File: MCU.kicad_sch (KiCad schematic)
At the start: 26 parts, among them U5 ESP32-D0WD, U6 W25Q128JVP, U7 APS6404L-3SQR-ZR, Y2 40.000 MHz

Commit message: updated Mouser part number for PSRAM
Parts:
- U7: MOUSER# 878-APS6404L-3SQR-ZR -> 878-APS6404L-3SQR-SN
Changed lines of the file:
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@@
 			)
 		)
-		(property "Datasheet" "~"
+		(property "Datasheet" "Data Sheets\\abm8-1384678.pdf"
 			(at 128.27 163.83 0)
 			(effects
@@
 			)
 		)
-		(property "Datasheet" "https://www.mouser.com/datasheet/2/1127/APM_PSRAM_QSPI_APS6404L_3SQR_v2_3_PKG-1954826.pdf"
+		(property "Datasheet" "Data Sheets\\APM_PSRAM_E3_QSPI__APS6404L_3SQR_KGD_PKG__v2.7.pdf"
 			(at 50.8 129.54 0)
 			(effects
@@
 			)
 		)
-		(property "MOUSER#" "878-APS6404L-3SQR-ZR"
+		(property "MOUSER#" "878-APS6404L-3SQR-SN"
 			(at 50.8 111.76 0)
 			(effects

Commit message: all parts geo-renamed
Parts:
- renumbered C49 to 1C10, C39 to 1C11, C38 to 1C12, R28 to 1R2, R45 to 1R3, R39 to 1R6, R41 to 1R8, U6 to 1U2, U5 to 1U4, C50 to 2C15, C22 to 2C16, C47 to 2C23, C20 to 2C26, C44 to 2C28, C48 to 2C29, C42 to 2C30, C19 to 2C31, C46 to 2C32, C41 to 2C33, C21 to 2C35, C45 to 2C36, C43 to 2C37, R42 to 2R20, R40 to 2R36, U7 to 2U3, Y2 to 2Y2
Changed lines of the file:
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@@
 		(on_board yes)
 		(dnp no)
-		(property "Reference" "C39"
+		(property "Reference" "1C11"
 			(at 116.84 44.4499 0)
 			(effects
@@
 			(project "ESP32PoE"
 				(path "/4c939de5-59ef-438d-9f29-5de1016e5f2f/9bdf3d9b-885e-428e-95ba-d4f7bd684dc5"
-					(reference "C39")
+					(reference "1C11")
 					(unit 1)
 				)
@@
 		(dnp no)
 		(fields_autoplaced yes)
-		(property "Reference" "C20"
+		(property "Reference" "2C26"
 			(at 139.7 171.4499 0)
 			(effects
@@
 			(project "ESP32PoE"
 				(path "/4c939de5-59ef-438d-9f29-5de1016e5f2f/9bdf3d9b-885e-428e-95ba-d4f7bd684dc5"
-					(reference "C20")
+					(reference "2C26")
 					(unit 1)
 				)
@@
 		(dnp no)
 		(fields_autoplaced yes)
-		(property "Reference" "R42"
+		(property "Reference" "2R20"
 			(at 39.37 96.5199 0)
 			(effects
@@
 			(project "ESP32PoE"
 				(path "/4c939de5-59ef-438d-9f29-5de1016e5f2f/9bdf3d9b-885e-428e-95ba-d4f7bd684dc5"
-					(reference "R42")
+					(reference "2R20")
 					(unit 1)
 				)
@@
 		(dnp no)
 		(fields_autoplaced yes)
-		(property "Reference" "Y2"
+		(property "Reference" "2Y2"
 			(at 139.7 157.4098 0)
 			(effects
@@
 			(project ""
 				(path "/4c939de5-59ef-438d-9f29-5de1016e5f2f/9bdf3d9b-885e-428e-95ba-d4f7bd684dc5"
-					(reference "Y2")
+					(reference "2Y2")
 					(unit 1)
 				)
@@
 		(dnp no)
 		(fields_autoplaced yes)
-		(property "Reference" "U5"
+		(property "Reference" "1U4"
 			(at 218.44 29.21 0)
 			(effects
@@
 			(project ""
 				(path "/4c939de5-59ef-438d-9f29-5de1016e5f2f/9bdf3d9b-885e-428e-95ba-d4f7bd684dc5"
-					(reference "U5")
+					(reference "1U4")
 					(unit 1)
 				)
@@
 		(dnp no)
 		(fields_autoplaced yes)
-		(property "Reference" "C38"
+		(property "Reference" "1C12"
 			(at 191.77 41.9099 0)
 			(effects
@@
 			(project "ESP32PoE"
 				(path "/4c939de5-59ef-438d-9f29-5de1016e5f2f/9bdf3d9b-885e-428e-95ba-d4f7bd684dc5"
-					(reference "C38")
+					(reference "1C12")
 					(unit 1)
 				)
@@
 		(dnp no)
 		(fields_autoplaced yes)
-		(property "Reference" "R28"
+		(property "Reference" "1R2"
 			(at 264.16 91.44 90)
 			(effects
@@
 			(project "ESP32PoE"
 				(path "/4c939de5-59ef-438d-9f29-5de1016e5f2f/9bdf3d9b-885e-428e-95ba-d4f7bd684dc5"
-					(reference "R28")
+					(reference "1R2")
 					(unit 1)
 				)
@@
 		(on_board yes)
 		(dnp no)
-		(property "Reference" "C21"
+		(property "Reference" "2C35"
 			(at 121.92 113.0299 0)
 			(effects
@@
 			(project "ESP32PoE"
 				(path "/4c939de5-59ef-438d-9f29-5de1016e5f2f/9bdf3d9b-885e-428e-95ba-d4f7bd684dc5"
-					(reference "C21")
+					(reference "2C35")
 					(unit 1)
 				)
@@
 		(dnp no)
 		(fields_autoplaced yes)
-		(property "Reference" "C49"
+		(property "Reference" "1C10"
 			(at 127 44.4499 0)
 			(effects
@@
 			(project "ESP32PoE"
 				(path "/4c939de5-59ef-438d-9f29-5de1016e5f2f/9bdf3d9b-885e-428e-95ba-d4f7bd684dc5"
-					(reference "C49")
+					(reference "1C10")
 					(unit 1)
 				)
@@
 		(on_board yes)
 		(dnp no)
-		(property "Reference" "C45"
+		(property "Reference" "2C36"
 			(at 33.02 59.6899 0)
 			(effects
@@
 			(project "ESP32PoE"
 				(path "/4c939de5-59ef-438d-9f29-5de1016e5f2f/9bdf3d9b-885e-428e-95ba-d4f7bd684dc5"
-					(reference "C45")
+					(reference "2C36")
 					(unit 1)
 				)
@@
 		(on_board yes)
 		(dnp no)
-		(property "Reference" "C19"
+		(property "Reference" "2C31"
 			(at 112.014 171.45 0)
 			(effects
@@
 			(project ""
 				(path "/4c939de5-59ef-438d-9f29-5de1016e5f2f/9bdf3d9b-885e-428e-95ba-d4f7bd684dc5"
-					(reference "C19")
+					(reference "2C31")
 					(unit 1)
 				)
@@
 		(dnp no)
 		(fields_autoplaced yes)
-		(property "Reference" "R39"
+		(property "Reference" "1R6"
 			(at 114.3 157.48 90)
 			(effects
@@
 			(project ""
 				(path "/4c939de5-59ef-438d-9f29-5de1016e5f2f/9bdf3d9b-885e-428e-95ba-d4f7bd684dc5"
-					(reference "R39")
+					(reference "1R6")
 					(unit 1)
 				)
@@
 		(on_board yes)
 		(dnp no)
-		(property "Reference" "C22"
+		(property "Reference" "2C16"
 			(at 139.7 44.4499 0)
 			(effects
@@
 			(project "ESP32PoE"
 				(path "/4c939de5-59ef-438d-9f29-5de1016e5f2f/9bdf3d9b-885e-428e-95ba-d4f7bd684dc5"
-					(reference "C22")
+					(reference "2C16")
 					(unit 1)
 				)
@@
 		(dnp no)
 		(fields_autoplaced yes)
-		(property "Reference" "U7"
+		(property "Reference" "2U3"
 			(at 59.69 110.4899 0)
 			(effects
@@
 			(project ""
 				(path "/4c939de5-59ef-438d-9f29-5de1016e5f2f/9bdf3d9b-885e-428e-95ba-d4f7bd684dc5"
-					(reference "U7")
+					(reference "2U3")
 					(unit 1)
 				)
@@
 		(dnp no)
 		(fields_autoplaced yes)
-		(property "Reference" "R40"
+		(property "Reference" "2R36"
 			(at 120.65 102.8699 0)
 			(effects
@@
 			(project "ESP32PoE"
 				(path "/4c939de5-59ef-438d-9f29-5de1016e5f2f/9bdf3d9b-885e-428e-95ba-d4f7bd684dc5"
-					(reference "R40")
+					(reference "2R36")
 					(unit 1)
 				)
@@
 		(dnp no)
 		(fields_autoplaced yes)
-		(property "Reference" "C42"
+		(property "Reference" "2C30"
 			(at 45.72 36.8299 0)
 			(effects
@@
 			(project "ESP32PoE"
 				(path "/4c939de5-59ef-438d-9f29-5de1016e5f2f/9bdf3d9b-885e-428e-95ba-d4f7bd684dc5"
-					(reference "C42")
+					(reference "2C30")
 					(unit 1)
 				)
@@
 		(on_board yes)
 		(dnp no)
-		(property "Reference" "C43"
+		(property "Reference" "2C37"
 			(at 71.12 36.8299 0)
 			(effects
@@
 			(project "ESP32PoE"
 				(path "/4c939de5-59ef-438d-9f29-5de1016e5f2f/9bdf3d9b-885e-428e-95ba-d4f7bd684dc5"
-					(reference "C43")
+					(reference "2C37")
 					(unit 1)
 				)
@@
 		(dnp no)
 		(fields_autoplaced yes)
-		(property "Reference" "C50"
+		(property "Reference" "2C15"
 			(at 149.86 44.4499 0)
 			(effects
@@
 			(project "ESP32PoE"
 				(path "/4c939de5-59ef-438d-9f29-5de1016e5f2f/9bdf3d9b-885e-428e-95ba-d4f7bd684dc5"
-					(reference "C50")
+					(reference "2C15")
 					(unit 1)
 				)
@@
 		(dnp no)
 		(fields_autoplaced yes)
-		(property "Reference" "C41"
+		(property "Reference" "2C33"
 			(at 33.02 36.8299 0)
 			(effects
@@
 			(project "ESP32PoE"
 				(path "/4c939de5-59ef-438d-9f29-5de1016e5f2f/9bdf3d9b-885e-428e-95ba-d4f7bd684dc5"
-					(reference "C41")
+					(reference "2C33")
 					(unit 1)
 				)
@@
 		(dnp no)
 		(fields_autoplaced yes)
-		(property "Reference" "R45"
+		(property "Reference" "1R3"
 			(at 177.8 118.1099 0)
 			(effects
@@
 			(project "ESP32PoE"
 				(path "/4c939de5-59ef-438d-9f29-5de1016e5f2f/9bdf3d9b-885e-428e-95ba-d4f7bd684dc5"
-					(reference "R45")
+					(reference "1R3")
 					(unit 1)
 				)
@@
 		(dnp no)
 		(fields_autoplaced yes)
-		(property "Reference" "C47"
+		(property "Reference" "2C23"
 			(at 74.93 58.4199 0)
 			(effects
@@
 			(project "ESP32PoE"
 				(path "/4c939de5-59ef-438d-9f29-5de1016e5f2f/9bdf3d9b-885e-428e-95ba-d4f7bd684dc5"
-					(reference "C47")
+					(reference "2C23")
 					(unit 1)
 				)
@@
 		(dnp no)
 		(fields_autoplaced yes)
-		(property "Reference" "C44"
+		(property "Reference" "2C28"
 			(at 58.42 36.8299 0)
 			(effects
@@
 			(project "ESP32PoE"
 				(path "/4c939de5-59ef-438d-9f29-5de1016e5f2f/9bdf3d9b-885e-428e-95ba-d4f7bd684dc5"
-					(reference "C44")
+					(reference "2C28")
 					(unit 1)
 				)
@@
 		(dnp no)
 		(fields_autoplaced yes)
-		(property "Reference" "R41"
+		(property "Reference" "1R8"
 			(at 190.5 128.2699 0)
 			(effects
@@
 			(project "ESP32PoE"
 				(path "/4c939de5-59ef-438d-9f29-5de1016e5f2f/9bdf3d9b-885e-428e-95ba-d4f7bd684dc5"
-					(reference "R41")
+					(reference "1R8")
 					(unit 1)
 				)
@@
 		(dnp no)
 		(fields_autoplaced yes)
-		(property "Reference" "C46"
+		(property "Reference" "2C32"
 			(at 44.45 59.6899 0)
 			(effects
@@
 			(project "ESP32PoE"
 				(path "/4c939de5-59ef-438d-9f29-5de1016e5f2f/9bdf3d9b-885e-428e-95ba-d4f7bd684dc5"
-					(reference "C46")
+					(reference "2C32")
 					(unit 1)
 				)
@@
 		(on_board yes)
 		(dnp no)
-		(property "Reference" "C48"
+		(property "Reference" "2C29"
 			(at 60.96 58.4199 0)
 			(effects
@@
 			(project "ESP32PoE"
 				(path "/4c939de5-59ef-438d-9f29-5de1016e5f2f/9bdf3d9b-885e-428e-95ba-d4f7bd684dc5"
-					(reference "C48")
+					(reference "2C29")
 					(unit 1)
 				)
@@
 		(dnp no)
 		(fields_autoplaced yes)
-		(property "Reference" "U6"
+		(property "Reference" "1U2"
 			(at 53.34 152.4 0)
 			(effects
@@
 			(project ""
 				(path "/4c939de5-59ef-438d-9f29-5de1016e5f2f/9bdf3d9b-885e-428e-95ba-d4f7bd684dc5"
-					(reference "U6")
+					(reference "1U2")
 					(unit 1)
 				)

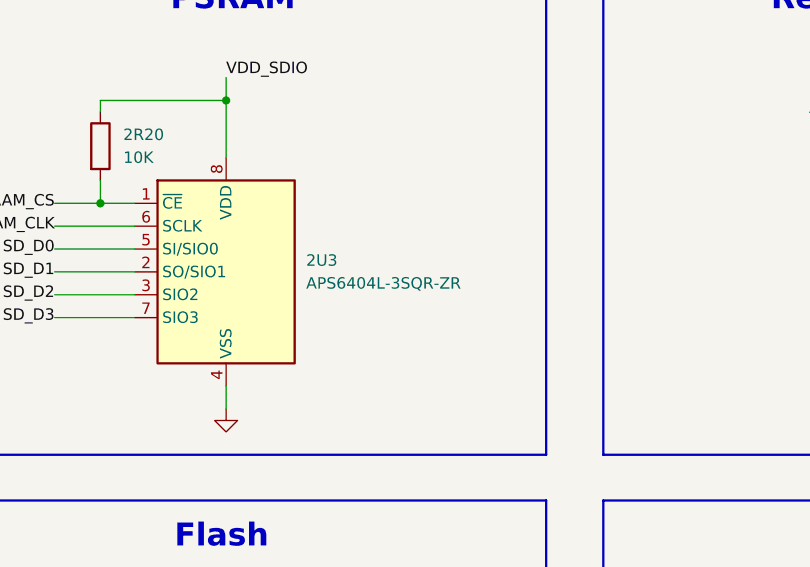
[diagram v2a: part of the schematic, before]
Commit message: fixed PSRAM part value
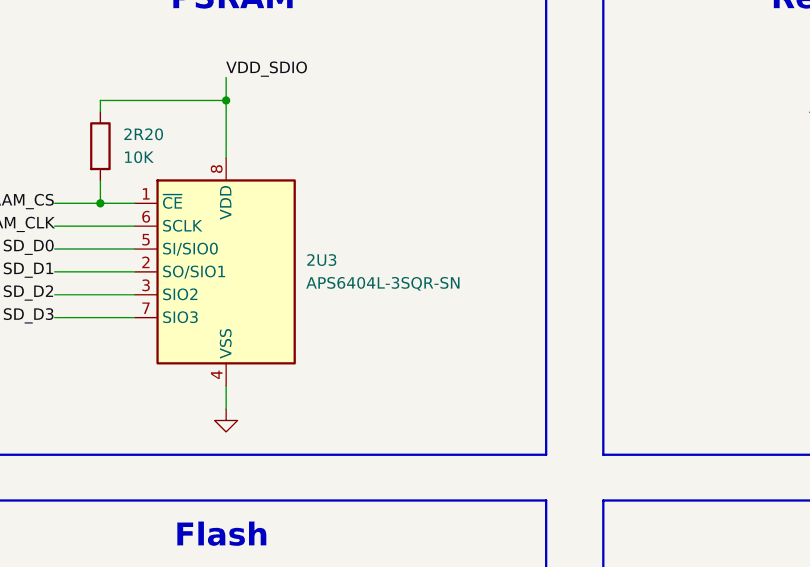
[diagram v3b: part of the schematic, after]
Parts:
- 2U3: value APS6404L-3SQR-ZR -> APS6404L-3SQR-SN
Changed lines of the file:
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@@
 			)
 		)
-		(property "Value" "APS6404L-3SQR-ZR"
+		(property "Value" "APS6404L-3SQR-SN"
 			(at 59.69 113.0299 0)
 			(effects

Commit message: properties cleanup added unique parts ID
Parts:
- 1C10, 2C15, 2C23, 2C28, 2C29, 2C30, 2C32, 2C33: IDAnything (none) -> 5cec8xb21wkrn9jazn0tx4yt0k
- 1C11, 2C16, 2C35, 2C36, 2C37: IDAnything (none) -> e5kfcvbxymkwra6w8qtzj3bv2h
- 1C12: IDAnything (none) -> bxzbaywtstgjdb4bw6yay3xr4b
- 1R2, 1R3, 1R6: IDAnything (none) -> ftsp2a555thn6bt15g7x2jan0j
- 1R8: IDAnything (none) -> 9p42scdygwgwrb2y4eq9ka8qyv
- 1U2: IDAnything (none) -> 2mpmsgq374g4187q6927v8vjqm
- 1U4: Availability In Stock -> (none); Check_prices https://www.snapeda.com/parts/ESP32-D0WD/Espressif+Systems/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 -> (none); Description_1 IC RF TxRx + MCU Bluetooth, WiFi 802.11b/g/n, Bluetooth 4.2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 -> (none); IDAnything (none) -> 8hr5rfs7grjc2bc0ndrafzzgq3; MANUFACTURER Expressif Systems -> (none); MF Espressif Systems -> (none); MP ESP32-D0WD -> (none); PACKAGE QFN-48 -> (none); PARTREV 1.7 -> (none); Package VFQFN-48 Espressif Systems -> (none); Price None -> (none); STANDARD IPC 7351B -> (none); SnapEDA_Link https://www.snapeda.com/parts/ESP32-D0WD/Espressif+Systems/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 -> (none)
- 2C26, 2C31: IDAnything (none) -> 9k9n51ff0ghzyb2jwxtjvng3h9
- 2R20, 2R36: IDAnything (none) -> c1vc3q1ecwg38aepd291cy2avj
- 2U3: IDAnything (none) -> 9xdwsqxw9chga8hnqmyxcamfjp
- 2Y2: IDAnything (none) -> 1q8m744mxek5h8d5ab7wa5xs8h

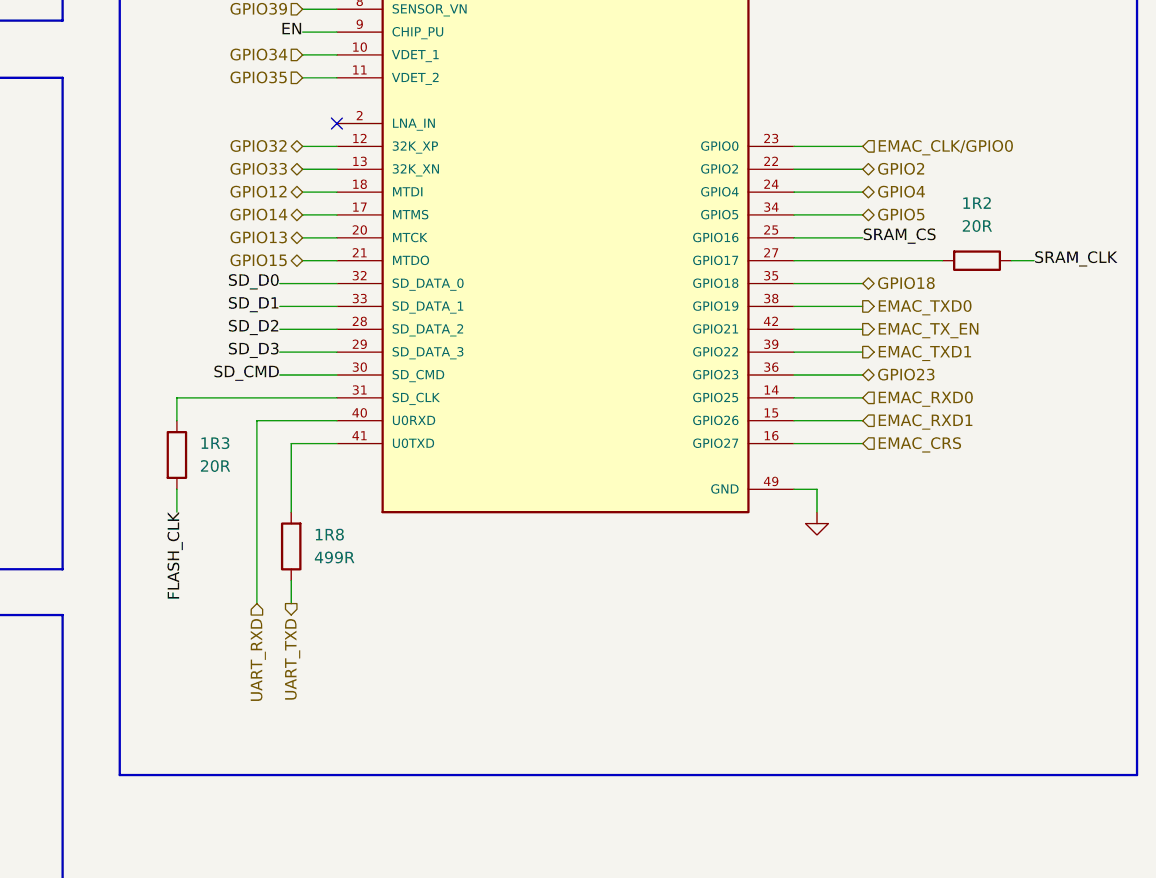
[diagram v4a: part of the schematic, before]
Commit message: added testpoints to flash/ram signals
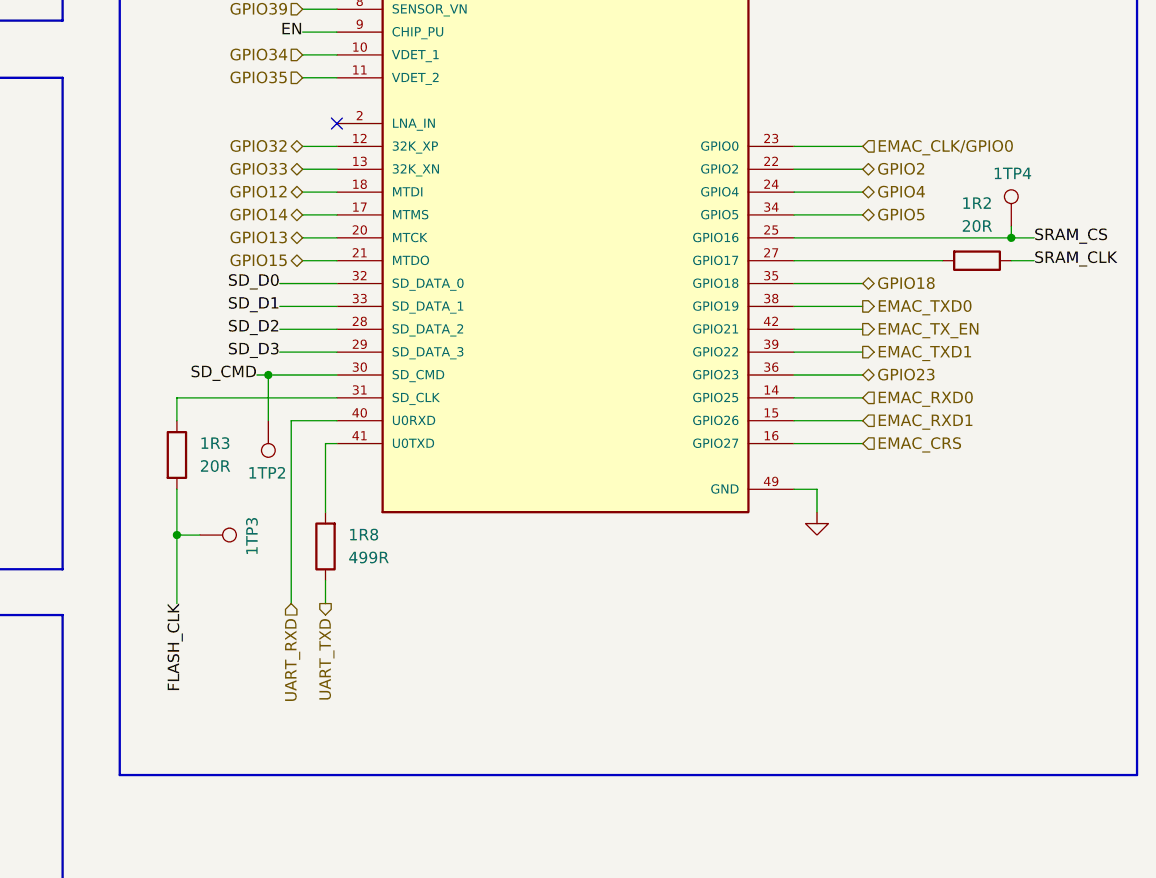
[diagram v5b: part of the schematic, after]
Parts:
- added 1TP2, 1TP3, 1TP4: TestPoint, TestPoint:TestPoint_Pad_D1.0mm, symbol Connector:TestPoint
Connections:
- net FLASH_CLK: now also 1TP3.1
- net SD_CMD: now also 1TP2.1
- net SRAM_CS: now also 1TP4.1
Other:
- moved on the sheet: 1R8
